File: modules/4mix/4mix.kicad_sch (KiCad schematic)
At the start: 39 parts, among them U1 MCP6002-xSN, U2 MCP6002-xSN, U3 MCP6002-xSN

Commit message: Add 4mix schematics
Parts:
- added C5, C6: 0.1uf, Capacitor_SMD:C_0402_1005Metric, symbol Device:C
- added GND2, V_SUPPLY2: Conn_01x05_Pin, BreadModular_MISC:Power_Connector, symbol Connector:Conn_01x05_Pin
- added INPUT2: Conn_01x02_Socket, Connector_PinSocket_2.54mm:PinSocket_1x02_P2.54mm_Vertical, symbol Connector:Conn_01x02_Socket
- added R21, R23, R29, R39: 1M, Resistor_SMD:R_0402_1005Metric, symbol Device:R
- added R22, R25, R27: 200k, Resistor_SMD:R_0402_1005Metric, symbol Device:R
- added R24, R26, R28: 1k, Resistor_SMD:R_0402_1005Metric, symbol Device:R
- added R40, R41, R42, R43: 100k, Resistor_SMD:R_0402_1005Metric, symbol Device:R
- added RV5, RV6, RV7: 50k, BreadModular_Pots:Potentiometer_RV09, symbol Device:R_Potentiometer
- added U4, U5: MCP6002-xSN, Package_SO:SOIC-8-1EP_3.9x4.9mm_P1.27mm_EP2.29x3mm, symbol Amplifier_Operational:MCP6002-xSN
- R12: value 1k -> 200k
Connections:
- net GND: now also C5.2, C6.2, GND2.1 (Pin_1), GND2.2 (Pin_2), GND2.3 (Pin_3), GND2.4 (Pin_4), GND2.5 (Pin_5), U4.4 (V-), U5.4 (V-)
- net MIXOUT: now also R26.2; no longer OUTPUT1.2 (Pin_2), OUTPUT1.3 (Pin_3), OUTPUT1.4 (Pin_4), OUTPUT1.5 (Pin_5), R12.2
- net V_MID: now also U3.5 (+), R29.1, R39.1, RV5.1, RV6.1, RV7.1, U4.3 (+), U4.5 (+), U5.3 (+), U5.5 (+)
- net V_SUPPLY: now also C5.1, C6.1, U4.8 (V+), U5.8 (V+), V_SUPPLY2.1 (Pin_1), V_SUPPLY2.2 (Pin_2), V_SUPPLY2.3 (Pin_3), V_SUPPLY2.4 (Pin_4), V_SUPPLY2.5 (Pin_5)
- net SENDS2/INPUT: now reaches R4.1, RV3.2
- net SENDS3/INPUT: now reaches R6.1, RV4.2
- net MAIN_MIX: now reaches R10.2, R11.1, R4.2, R6.2, R8.2, U3.2 (-)
- net at R11.2, U3.1: now also RV5.3; no longer R12.1
- net SEND_A_MIX: now reaches U3.6 (-)
- net SEND_A_MIX: now also R21.1
- net at U3.7: now also R21.2, R24.1
- net SENDS/INPUT: now reaches R8.1, RV1.2
- net SENDS1/INPUT: now reaches R10.1, RV2.2
- new net: R27.1, RV5.2
- new net: R12.2, R22.2, R25.1, R27.2, U4.6 (-)
- new net: R22.1, RV7.2
- new net: R42.2, R43.1, U5.6 (-)
- new net: R43.2, RV7.3, U5.7
- new net: R23.2, R28.1, U4.1
- new net: R12.1, RV6.2
- new net: R40.2, R41.1, U5.2 (-)
- new net: R41.2, RV6.3, U5.1
- new net OD_CLEAN: OUTPUT1.2 (Pin_2)
- new net OD_DIRTY: OUTPUT1.3 (Pin_3)
- new net Overdrive/INPUT: R25.2, R26.1, U4.7
- new net RETURN_A: INPUT2.1 (Pin_1), R39.2, R40.1
- new net RETURN_B: INPUT2.2 (Pin_2), R29.2, R42.1
- new net SEND_A_OUT: OUTPUT1.4 (Pin_4), R24.2
- new net SEND_B_MIX: R23.1, U4.2 (-)
- new net SEND_B_OUT: OUTPUT1.5 (Pin_5), R28.2
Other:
- added sheet Overdrive (overdrive.kicad_sch)
- added sheet SENDS (sends.kicad_sch)
- added sheet SENDS1 (sends.kicad_sch)
- added sheet SENDS2 (sends.kicad_sch)
- added sheet SENDS3 (sends.kicad_sch)
- moved on the sheet: C1, C2, C3, C4, GND1, INPUT1, OUTPUT1, R1, R10, R11, R2, R4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

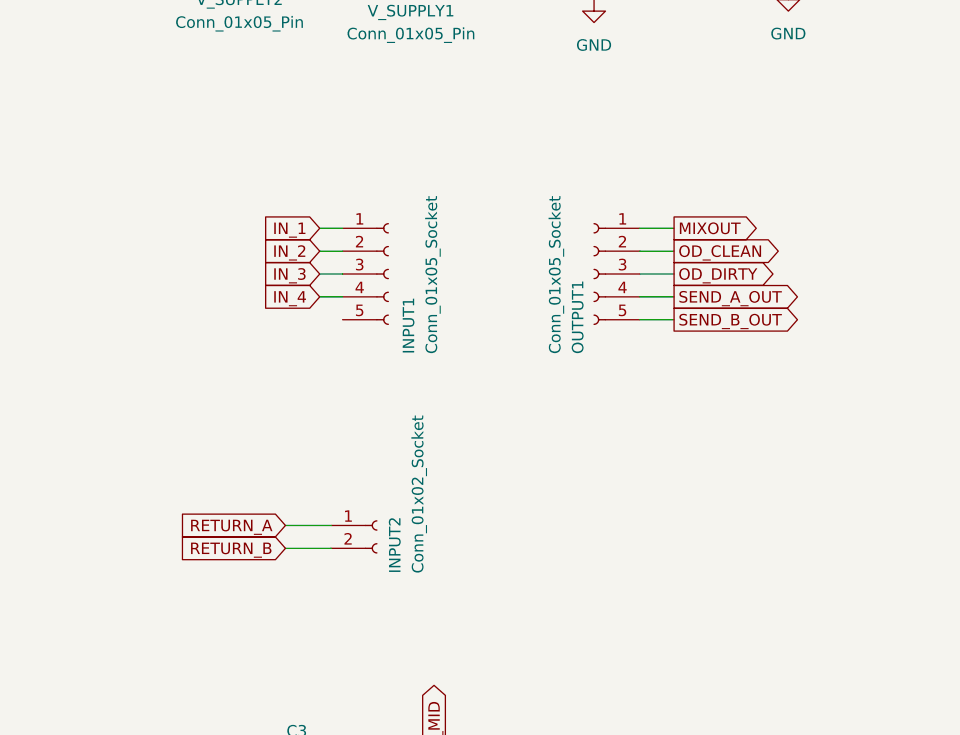
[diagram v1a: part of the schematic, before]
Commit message: Finished all the routing
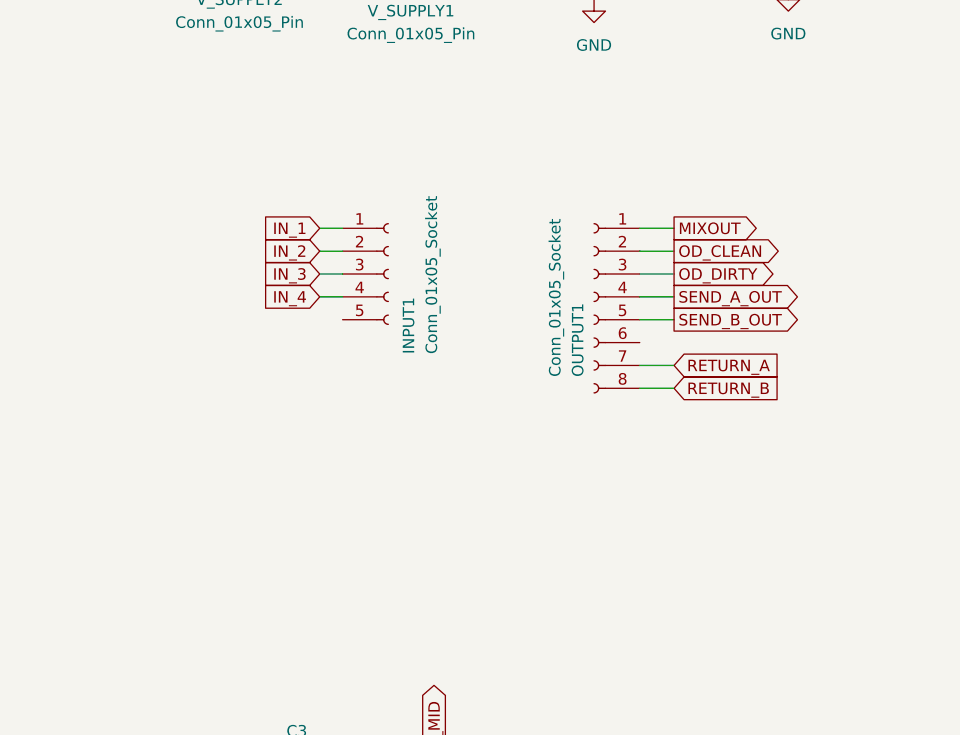
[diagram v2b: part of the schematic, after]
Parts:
- removed INPUT2: Conn_01x02_Socket, Connector_PinSocket_2.54mm:PinSocket_1x02_P2.54mm_Vertical, symbol Connector:Conn_01x02_Socket
- removed OUTPUT1: Conn_01x05_Socket, Connector_PinSocket_2.54mm:PinSocket_1x05_P2.54mm_Vertical, symbol Connector:Conn_01x05_Socket
- added OUTPUT1: Conn_01x05_Socket, Connector_PinSocket_2.54mm:PinSocket_1x08_P2.54mm_Vertical, symbol Connector:Conn_01x08_Socket
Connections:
- net MIXOUT: now also OUTPUT1.1 (Pin_1)
- net OD_CLEAN: now also OUTPUT1.2 (Pin_2)
- net OD_DIRTY: now also OUTPUT1.3 (Pin_3)
- net RETURN_A: now also OUTPUT1.7 (Pin_7)
- net RETURN_B: now also OUTPUT1.8 (Pin_8)
- net SEND_A_OUT: now also OUTPUT1.4 (Pin_4)
- net SEND_B_OUT: now also OUTPUT1.5 (Pin_5)
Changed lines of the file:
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@@
 	(wire
 		(pts
-			(xy 496.57 105.41) (xy 501.65 105.41)
+			(xy 539.75 87.63) (xy 535.94 87.63)
 		)
 		(stroke
@@
 	(wire
 		(pts
-			(xy 496.57 107.95) (xy 501.65 107.95)
+			(xy 539.75 90.17) (xy 535.94 90.17)
 		)
 		(stroke
@@
 	(global_label "RETURN_A"
 		(shape input)
-		(at 496.57 105.41 180)
+		(at 539.75 87.63 0)
 		(fields_autoplaced yes)
 		(effects
@@
 				(size 1.27 1.27)
 			)
-			(justify right)
+			(justify left)
 		)
 		(property "Intersheetrefs" "${INTERSHEET_REFS}"
-			(at 484.211 105.41 0)
+			(at 552.109 87.63 0)
 			(effects
 				(font
 					(size 1.27 1.27)
 				)
-				(justify right)
+				(justify left)
 				(hide yes)
 			)
@@
 	(global_label "RETURN_B"
 		(shape input)
-		(at 496.57 107.95 180)
+		(at 539.75 90.17 0)
 		(fields_autoplaced yes)
 		(effects
@@
 				(size 1.27 1.27)
 			)
-			(justify right)
+			(justify left)
 		)
 		(property "Intersheetrefs" "${INTERSHEET_REFS}"
-			(at 484.0296 107.95 0)
+			(at 552.2904 90.17 0)
 			(effects
 				(font
 					(size 1.27 1.27)
 				)
-				(justify right)
+				(justify left)
 				(hide yes)
 			)
@@
 	)
 	(symbol
-		(lib_id "Connector:Conn_01x02_Socket")
-		(at 506.73 105.41 0)
-		(unit 1)
-		(exclude_from_sim yes)
-		(in_bom yes)
-		(on_board yes)
-		(dnp no)
-		(property "Reference" "INPUT2"
-			(at 508.762 110.744 90)
-			(effects
-				(font
-					(size 1.27 1.27)
-				)
-				(justify left)
-			)
-		)
-		(property "Value" "Conn_01x02_Socket"
-			(at 511.302 110.744 90)
-			(effects
-				(font
-					(size 1.27 1.27)
-				)
-				(justify left)
-			)
-		)
-		(property "Footprint" "Connector_PinSocket_2.54mm:PinSocket_1x02_P2.54mm_Vertical"
-			(at 506.73 105.41 0)
-			(effects
-				(font
-					(size 1.27 1.27)
-				)
-				(hide yes)
-			)
-		)
-		(property "Datasheet" "~"
-			(at 506.73 105.41 0)
-			(effects
-				(font
-					(size 1.27 1.27)
-				)
-				(hide yes)
-			)
-		)
-		(property "Description" "Generic connector, single row, 01x02, script generated"
-			(at 506.73 105.41 0)
-			(effects
-				(font
-					(size 1.27 1.27)
-				)
-				(hide yes)
-			)
-		)
-		(pin "2"
-		)
-		(pin "1"
-		)
-		(instances
-			(project "4mix"
-				(path "/b63493d3-5f6d-47e3-845b-87e7090fc1ab"
-					(reference "INPUT2")
-					(unit 1)
-				)
-			)
-		)
-	)
-	(symbol
 		(lib_id "Device:C")
 		(at 505.46 177.8 0)
@@
 	)
 	(symbol
-		(lib_id "Connector:Conn_01x05_Socket")
-		(at 530.86 77.47 0)
-		(mirror y)
-		(unit 1)
-		(exclude_from_sim yes)
-		(in_bom yes)
-		(on_board yes)
-		(dnp no)
-		(property "Reference" "OUTPUT1"
-			(at 529.082 86.36 90)
-			(effects
-				(font
-					(size 1.27 1.27)
-				)
-				(justify left)
-			)
-		)
-		(property "Value" "Conn_01x05_Socket"
-			(at 526.542 86.36 90)
-			(effects
-				(font
-					(size 1.27 1.27)
-				)
-				(justify left)
-			)
-		)
-		(property "Footprint" "Connector_PinSocket_2.54mm:PinSocket_1x05_P2.54mm_Vertical"
-			(at 530.86 77.47 0)
-			(effects
-				(font
-					(size 1.27 1.27)
-				)
-				(hide yes)
-			)
-		)
-		(property "Datasheet" "~"
-			(at 530.86 77.47 0)
-			(effects
-				(font
-					(size 1.27 1.27)
-				)
-				(hide yes)
-			)
-		)
-		(property "Description" "Generic connector, single row, 01x05, script generated"
-			(at 530.86 77.47 0)
-			(effects
-				(font
-					(size 1.27 1.27)
-				)
-				(hide yes)
-			)
-		)
-		(pin "3"
-		)
-		(pin "2"
-		)
-		(pin "1"
-		)
-		(pin "5"
-		)
-		(pin "4"
-		)
-		(instances
-			(project "blank"
-				(path "/b63493d3-5f6d-47e3-845b-87e7090fc1ab"
-					(reference "OUTPUT1")
-					(unit 1)
-				)
-			)
-		)
-	)
-	(symbol
 		(lib_id "Connector:Conn_01x05_Pin")
 		(at 491.49 44.45 90)
@@
 				)
 			)
+		)
+	)
+	(symbol
+		(lib_id "Connector:Conn_01x08_Socket")
+		(at 530.86 80.01 0)
+		(mirror y)
+		(unit 1)
+		(exclude_from_sim no)
+		(in_bom yes)
+		(on_board yes)
+		(dnp no)
+		(property "Reference" "OUTPUT1"
+			(at 529.082 88.9 90)
+			(effects
+				(font
+					(size 1.27 1.27)
+				)
+				(justify left)
+			)
+		)
+		(property "Value" "Conn_01x05_Socket"
+			(at 526.542 88.9 90)
+			(effects
+				(font
+					(size 1.27 1.27)
+				)
+				(justify left)
+			)
+		)
+		(property "Footprint" "Connector_PinSocket_2.54mm:PinSocket_1x08_P2.54mm_Vertical"
+			(at 530.86 80.01 0)
+			(effects
+				(font
+					(size 1.27 1.27)
+				)
+				(hide yes)
+			)
+		)
+		(property "Datasheet" "~"
+			(at 530.86 80.01 0)
+			(effects
+				(font
+					(size 1.27 1.27)
+				)
+				(hide yes)
+			)
+		)
+		(property "Description" "Generic connector, single row, 01x08, script generated"
+			(at 530.86 80.01 0)
+			(effects
+				(font
+					(size 1.27 1.27)
+				)
+				(hide yes)
+			)
+		)
+		(pin "3"
+		)
+		(pin "2"
+		)
+		(pin "1"
+		)
+		(pin "5"
+		)
+		(pin "4"
+		)
+		(pin "6"
+		)
+		(pin "7"
+		)
+		(pin "8"
+		)
+		(instances
+			(project "4mix"
+				(path "/b63493d3-5f6d-47e3-845b-87e7090fc1ab"
+					(reference "OUTPUT1")
+					(unit 1)
+				)
+			)

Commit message: Fix phase issues & cascading support. * There were some phase issues related when mixing returns   in the master mixer. * Now input and mixout has the same phase * Add in_mixout, in_send_a & in_send_b to cascase another mixser
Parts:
- removed R41, R43: 100k, Resistor_SMD:R_0402_1005Metric, symbol Device:R
- removed unit 1 of U3
- removed unit 2 of U3
- removed unit 1 of U4
- removed unit 2 of U4
- added C5, C7: 0.1uf, Capacitor_SMD:C_0402_1005Metric, symbol Device:C
- added R1, R31, R32, R39, R40: 1M, Resistor_SMD:R_0402_1005Metric, symbol Device:R
- added R15, R30, R33, R34, R35, R36, R37, R6: 100k, Resistor_SMD:R_0402_1005Metric, symbol Device:R
- added R23: 200k, Resistor_SMD:R_0402_1005Metric, symbol Device:R
- added U2, U6: MCP6002-xSN, Package_SO:SOIC-8-1EP_3.9x4.9mm_P1.27mm_EP2.29x3mm, symbol Amplifier_Operational:MCP6002-xSN
- added unit 2 of U5
- added unit 1 of U5
- added unit 2 of U7
- added unit 1 of U7
- added V5: VSIN, symbol Simulation_SPICE:VSIN
- INPUT1: footprint Connector_PinSocket_2.54mm:PinSocket_1x05_P2.54mm_Vertical -> Connector_PinSocket_2.54mm:PinSocket_1x08_P2.54mm_Vertical; symbol Connector:Conn_01x05_Socket -> Connector:Conn_01x08_Socket
- renumbered C2 to C1, C6 to C2, C1 to C3, C3 to C4, C4 to C6, C5 to C8, R14 to R10, R40 to R11, R42 to R12, R17 to R13, R19 to R14, R13 to R16, R15 to R17, R39 to R18, R29 to R19, R3 to R2, R11 to R20, R4 to R21, R6 to R22, R8 to R24, R10 to R25, R27 to R26, R12 to R27, R22 to R28, R25 to R29, R5 to R3, R26 to R38, R9 to R4, R21 to R41, R23 to R42, R24 to R43, R28 to R44, R1 to R45, R2 to R46, R7 to R5, R20 to R7, R18 to R8, R16 to R9, RV3 to RV1, RV4 to RV2, RV1 to RV3, RV2 to RV4, U2 to U1, U1 to U3, U5 to U4, U4 to U5, U3 to U7, V_SUPPLY2 to V_SUPPLY1, V_SUPPLY1 to V_SUPPLY2
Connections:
- net GND: now also C5.2, C7.2, U2.4 (V-), U6.4 (V-), V5.2
- net MAIN_MIX: now also R23.2, U2.6 (-)
- net Overdrive/INPUT: now also R33.2, U5.7; no longer R29.2
- net RETURN_A: no longer R18.2
- net RETURN_B: no longer R19.2
- net SEND_A_MIX: now also R39.2, U7.2 (-)
- net SEND_B_MIX: now also R40.2, U7.6 (-)
- net V_MID: now also R1.1, R31.1, R32.1, U2.3 (+), U2.5 (+), U5.3 (+), U5.5 (+), U6.3 (+), U6.5 (+), U7.3 (+), U7.5 (+); no longer U4.3 (+), U4.5 (+)
- net V_SUPPLY: now also C5.1, C7.1, U2.8 (V+), U6.8 (V+)
- net at R26.2, R27.2, R28.2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: now also U5.2 (-)
- net at R20.2, RV5.3: now also U2.7
- net at R12.2: now also R19.2, U4.5 (+); no longer U4.6 (-)
- net at RV7.3, U4.7: now also U4.6 (-)
- net at R41.2, R43.1: now also U7.1
- net at R42.2, R44.1: now also U7.7
- net at R11.2: now also R18.2, U4.3 (+); no longer U4.2 (-)
- net at RV6.3, U4.1: now also U4.2 (-)
- new net: R15.2, R23.1, U2.1
- new net: R35.2, R37.1, U6.6 (-)
- new net: R34.2, R36.1, U6.2 (-)
- new net: R36.2, R39.1, U6.1
- new net: R37.2, R40.1, U6.7
- new net: R15.1, R6.2, U2.2 (-)
- new net: R29.2, R30.1, U5.1
- new net: R30.2, R33.1, U5.6 (-)
- new net IN_MIXOUT: INPUT1.6 (Pin_6), R1.2, R6.1
- new net IN_SEND_A: INPUT1.7 (Pin_7), R31.2, R34.1
- new net IN_SEND_B: INPUT1.8 (Pin_8), R32.2, R35.1
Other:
- note added: "# Channels"
- note added: "# Component Power"
- note added: "# IO"
- note added: "# Master Mix"
- note added: "# Overdrive"
- note added: "# Sends Mix"
- note added: "# Simulation Tools"
- note added: "Here we use non-inverting op-amp configuration to set the phase correct of returns. We set 100k resistor on the front to set the impedence correct. Also practically, non-inverting configuration is suspect to noise. Putting that 100k would prevent it."
- note added: "Sends and Returns are connected for the testing purpose."
- note added: "This opamp stage will buffer the input and set the phase correct for mixing."
- note added: "We use this inverting op-amp to set the phase correct as the input. Otherwise this will affect when we chaining multiple 4mixes."
- moved on the sheet: C1, C2, C3, C6, C8, R10, R11, R12, R13, R14, R16, R17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

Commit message: Add some improvements to 4mix
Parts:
- added C14, C15, C16, C17, C18, C19, C20: 47pf, Capacitor_SMD:C_0402_1005Metric, symbol Device:C
- added C21, C22: 100pf, Capacitor_SMD:C_0402_1005Metric, symbol Device:C
- added C23: 0.1uf, Capacitor_SMD:C_1206_3216Metric, symbol Device:C
- added R61, R62: 1M, Resistor_SMD:R_0402_1005Metric, symbol Device:R
- added R74, R75, R76, R77, R78: 100, Resistor_SMD:R_0402_1005Metric, symbol Device:R
- added R79: 10, Resistor_SMD:R_0402_1005Metric, symbol Device:R
- added RV18, RV19: 500k, BreadModular_Pots:Potentiometer_RV09, symbol Device:R_Potentiometer
- added U10: MCP6002-xSN, Package_SO:SOIC-8-1EP_3.9x4.9mm_P1.27mm_EP2.29x3mm, symbol Amplifier_Operational:MCP6002-xSN
- R11, R12: value 100k -> 10k
- R20, R26, R27, R28, R29: value 200k -> 56k
- R30, R33, R34, R35, R36, R37: value 100k -> 56k
- R39, R40, R41, R42: value 1M -> 56k
- R43, R44: value 1k -> 330; footprint Resistor_SMD:R_0402_1005Metric -> Resistor_SMD:R_0805_2012Metric
- R45, R46: value 1k -> 10k
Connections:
- net MAIN_MIX: now also C14.2
- net Overdrive/INPUT: now also C20.1
- net SEND_A_MIX: now also C17.2, R61.2
- net SEND_B_MIX: now also C18.2, R62.2
- net V_MID: now also C21.1, C22.1, R79.2, RV18.1, RV19.1; no longer C4.2, R45.2, R46.1
- net V_SUPPLY: no longer C4.1
- net at R26.2, R27.2, R28.2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: now also C19.2
- net at R35.2, R37.1, U6.6 (-): now also C16.2
- net at R34.2, R36.1, U6.2 (-): now also C15.2
- net at R11.2, R18.2, U4.3 (+): now also C21.2
- net at R20.2, U2.7: now also C14.1, R74.1; no longer RV5.3
- net at R42.2, R44.1, U7.7: now also C18.1
- net at R36.2, U6.1: now also C15.1, R77.1; no longer R39.1
- net at R37.2, U6.7: now also C16.1, R78.1; no longer R40.1
- net at R41.2, R43.1, U7.1: now also C17.1
- net at R12.2, R19.2, U4.5 (+): now also C22.2
- net at U4.6 (-), U4.7: now also R76.1; no longer RV7.3
- net at R29.2, R30.1, U5.1: now also C19.1
- net at U4.1, U4.2 (-): now also R75.1; no longer RV6.3
- net at R30.2, R33.1, U5.6 (-): now also C20.2
- net SENDS/INPUT: no longer names the net of R24.1, RV3.2
- net SENDS/INPUT: now also RV18.3, RV19.3
- new net: C23.1, C23.2, C4.1, C4.2, R45.2, R46.1, U10.5 (+)
- new net: R61.1, RV18.2
- new net: R79.1, U10.6 (-), U10.7
- new net: R74.2, RV5.3
- new net: R76.2, RV7.3
- new net: R62.1, RV19.2
- new net: R39.1, R77.2
- new net: R75.2, RV6.3
- new net: R40.1, R78.2
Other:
- removed sheet SENDS
- added sheet CHANNEL (channel.kicad_sch)
- note added: "Here we use non-inverting op-amp configuration to set the phase correct of returns. We set 4.6k resistor on the front to set the impedence correct. Also practically, non-inverting configuration is suspect to noise. Putting that 100k would prevent it."
- note added: "This sits close to the summing amp"
- note removed: "Here we use non-inverting op-amp configuration to set the phase correct of returns. We set 100k resistor on the front to set the impedence correct. Also practically, non-inverting configuration is suspect to noise. Putting that 100k would prevent it."
- moved on the sheet: C4, R12, R18, R39, R40, R46

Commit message: Finished the new schematic for 4mix
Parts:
- removed C1: 0.1uf, Capacitor_SMD:C_0402_1005Metric, symbol Device:C
- removed R10, R13, R14, R16, R17, R7, R8: 100k, Resistor_SMD:R_0402_1005Metric, symbol Device:R
- removed R2, R3, R4, R5, R61, R62: 1M, Resistor_SMD:R_0402_1005Metric, symbol Device:R
- removed R21, R22, R24, R25: 200k, Resistor_SMD:R_0402_1005Metric, symbol Device:R
- removed RV1, RV2, RV3, RV4: 50k, BreadModular_Pots:Potentiometer_RV09, symbol Device:R_Potentiometer
- removed RV18, RV19: 500k, BreadModular_Pots:Potentiometer_RV09, symbol Device:R_Potentiometer
- removed U1, U3: MCP6002-xSN, Package_SO:SOIC-8-1EP_3.9x4.9mm_P1.27mm_EP2.29x3mm, symbol Amplifier_Operational:MCP6002-xSN
- added C18: 0.1uf, Capacitor_SMD:C_0402_1005Metric, symbol Device:C
- added unit 3 of U6
- added unit 1 of U6
- C3: value 0.1uf -> 47pf
- R11: renamed from R23; value 200k -> 56k
- R2: renamed from R6; value 100k -> 56k
- R5: renamed from R15; value 100k -> 56k
- R9: value 100k -> 100
- renumbered C21 to C1, C18 to C10, C7 to C11, C5 to C12, C2 to C13, C6 to C14, C23 to C15, C4 to C16, C8 to C17, C22 to C2, C14 to C4, C19 to C5, C20 to C6, C15 to C7, C16 to C8, C17 to C9, R74 to R10, R75 to R12, R76 to R13, R26 to R14, R27 to R15, R28 to R16, R29 to R17, R30 to R18, R31 to R19, R32 to R20, R33 to R21, R34 to R22, R35 to R23, R36 to R24, R37 to R25, R38 to R26, R77 to R27, R78 to R28, R39 to R29, R11 to R3, R40 to R30, R41 to R31, R42 to R32, R43 to R33, R44 to R34, R45 to R35, R46 to R36, R79 to R37, R12 to R4, R18 to R6, R19 to R7, R20 to R8, RV5 to RV1, RV6 to RV2, RV7 to RV3, U2 to U1, U4 to U2, U5 to U3, U6 to U4, U7 to U5, U10 to U6
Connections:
- net GND: now also C18.2, U6.4 (V-); no longer C3.2
- net IN_2: no longer R9.1
- net V_SUPPLY: now also C18.1, U6.8 (V+); no longer C3.1
- net at R5.2, U1.1: now also C3.1, R9.1; no longer R11.1
- net at R9.2: now also R11.1
- net at R2.2, R5.1, U1.2 (-): now also C3.2
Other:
- removed sheet CHANNEL
- removed sheet SENDS1
- removed sheet SENDS2
- removed sheet SENDS3
- added sheet CHANNEL_1 (channel_1.kicad_sch)
- added sheet CHANNEL_2 (channel_2.kicad_sch)
- added sheet CHANNEL_3 (channel_3.kicad_sch)
- added sheet CHANNEL_4 (channel_4.kicad_sch)
- moved on the sheet: C11, C12, C13, C14, C17, R1, R11, R2, R5, U1A, U1C, U2C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

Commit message: Reconfigure the simulations
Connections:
- net IN_3: no longer V4.1
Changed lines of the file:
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@@
 	(wire
 		(pts
-			(xy 528.32 302.26) (xy 528.32 306.07)
-		)
-		(stroke
-			(width 0)
-			(type default)
-		)
-	)
-	(wire
-		(pts
 			(xy 350.52 140.97) (xy 350.52 128.27)
 		)
@@
 	(wire
 		(pts
-			(xy 487.68 302.26) (xy 487.68 306.07)
-		)
-		(stroke
-			(width 0)
-			(type default)
-		)
-	)
-	(wire
-		(pts
 			(xy 318.77 300.99) (xy 326.39 300.99)
 		)
@@
 	(wire
 		(pts
+			(xy 487.68 302.26) (xy 487.68 306.07)
+		)
+		(stroke
+			(width 0)
+			(type default)
+		)
+	)
+	(wire
+		(pts
 			(xy 505.46 226.06) (xy 505.46 229.87)
 		)
@@
 	(wire
 		(pts
+			(xy 509.27 302.26) (xy 509.27 306.07)
+		)
+		(stroke
+			(width 0)
+			(type default)
+		)
+	)
+	(wire
+		(pts
 			(xy 513.08 111.76) (xy 538.48 111.76)
 		)
@@
 	(wire
 		(pts
-			(xy 509.27 302.26) (xy 509.27 306.07)
-		)
-		(stroke
-			(width 0)
-			(type default)
-		)
-	)
-	(wire
-		(pts
 			(xy 133.35 283.21) (xy 139.7 283.21)
 		)
@@
 			)
 		)
-		(property "Sim.Params" "dc=1.65 ampl=1.65 f=15k ac=1"
+		(property "Sim.Params" "dc=1.65 ampl=1.65 f=10k ac=1"
 			(at 536.956 322.072 90)
 			(effects
